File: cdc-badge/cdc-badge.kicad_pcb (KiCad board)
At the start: 4 copper layers, 85 x 110 mm, 159 parts, among them J1 USB_C, J2 JST S2B-PH-SM4-TB, J3 Conn_02x20_Odd_Even, J4 Conn_Grove, J5 Conn_02x03_Odd_Even, J6 Conn_01x06, J7 Conn_01x24, Q1 Si1308EDL, Q2 Si1308EDL, SW0 0, SW1 1, SW10 YES, SW11 NO, SW12 power on/reset, SW13 reset, SW14 flash/power off, SW15 MST-22D18G2 3J, SW16 MST-22D18G2 3J, SW17 MS-22D28-G020, SW2 2, SW3 3, SW4 4, SW5 5, SW6 6, SW7 7, SW8 8, SW9 9, U1 ESP32-S3-WROOM-1-N16R8, U2 TCA9535PWR, U3 TR01-C2P-T301, U5 TLV61070ADBVR, U6 BQ25895RTW, U7 USBLC6-2SC6, U8 TLV62569DBV

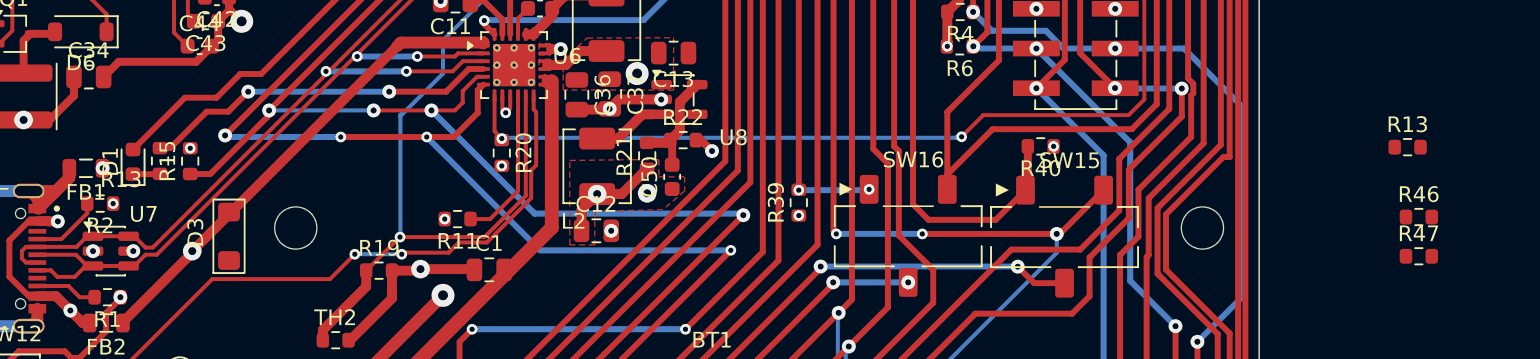
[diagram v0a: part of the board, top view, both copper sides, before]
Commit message: PCB: added R46 and R47 to allow hacking via S3 Pins CE and OTG
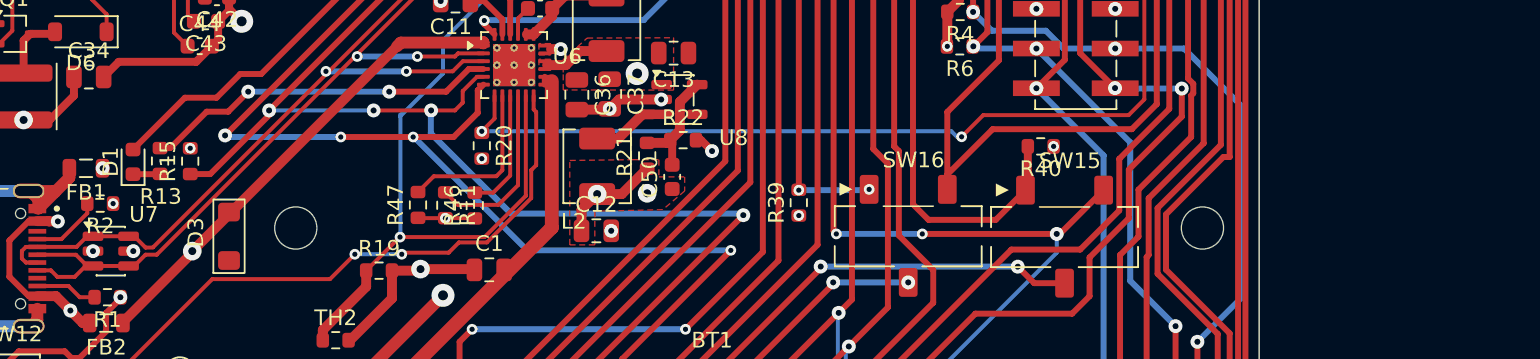
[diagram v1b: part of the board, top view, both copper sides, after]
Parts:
- removed the R13 at (118.2, 90.5)
- moved R47 64.1 mm to (54.9, 94.1), turned to 90 degrees
- moved R46 60.4 mm to (58.6, 94.2), turned to 90 degrees
- moved R20 1.36 mm to (59.0, 90.4)
- moved R11 1.18 mm to (56.7, 94.2), turned to -90 degrees
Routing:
- net Net-(U6-OTG): track 0.00 -> 10.7 mm
- net Net-(U6-~{CE}): track 0.00 -> 7.83 mm
- net Net-(U6-ILIM): track 9.88 -> 11.2 mm
- net GND: track 152.4 -> 153.7 mm, vias 38 -> 37
- net /CHG_IRQ: track 75.9 -> 76.9 mm
- net /I2C0_SCL: track 141.2 -> 142.1 mm
- net /I2C0_SDA: track 132.5 -> 133.3 mm

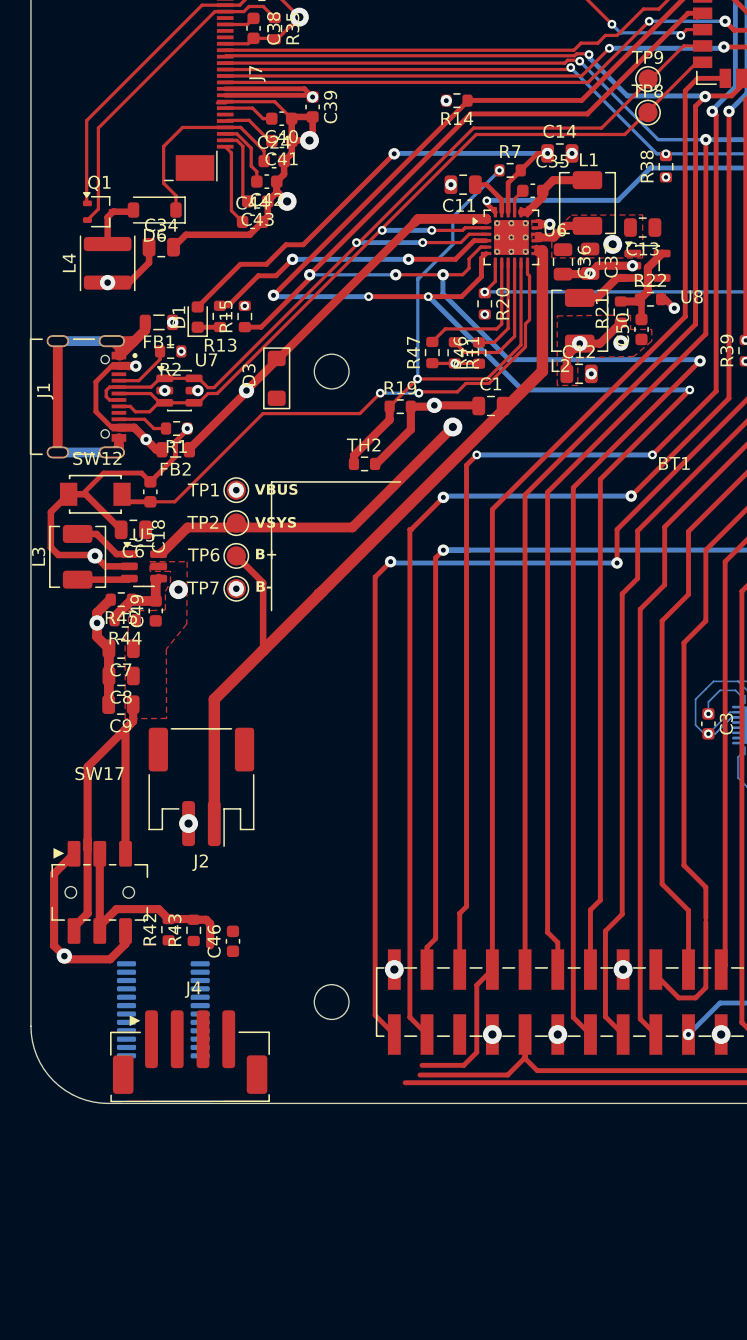
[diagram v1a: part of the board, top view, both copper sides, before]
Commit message: PCB: placed additional diodes and R's to Epaper connector
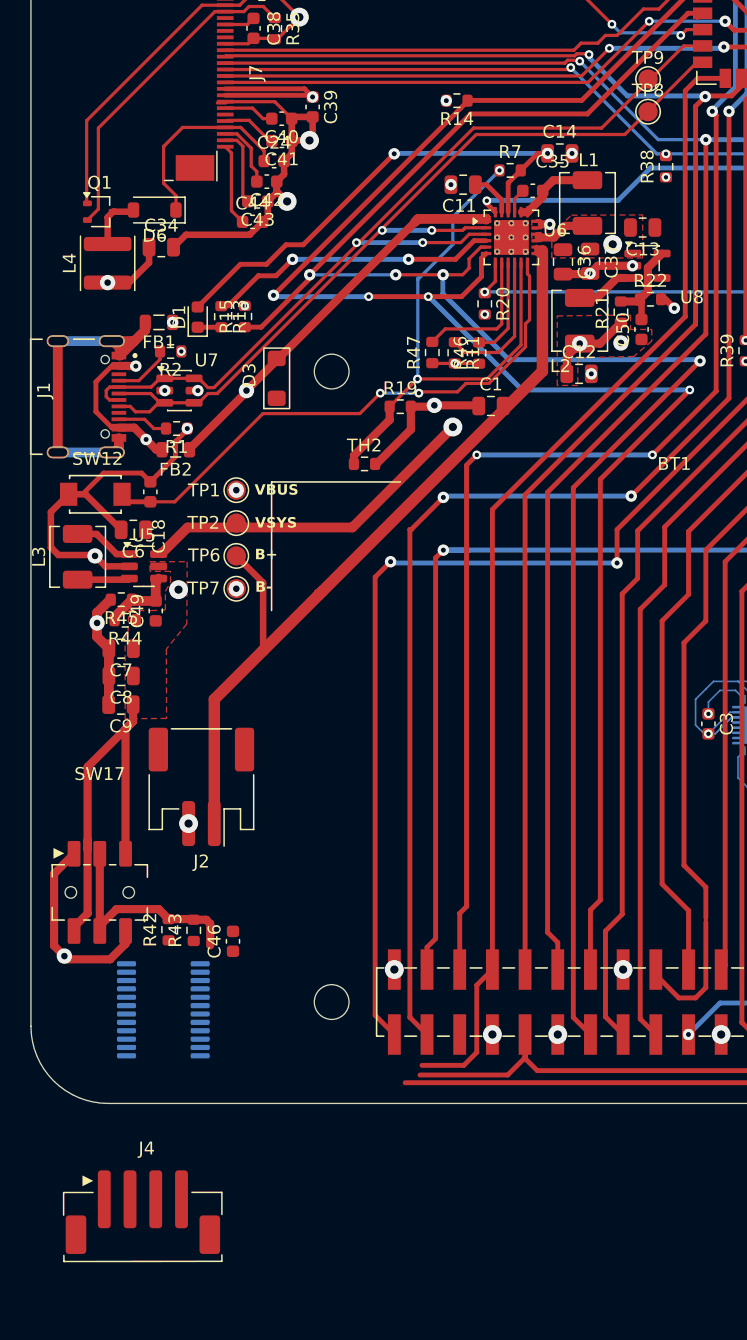
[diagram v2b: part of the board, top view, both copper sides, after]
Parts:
- R13: value 130 -> 5.1k
- moved J4 13.0 mm to (32.5, 162.1)
- moved R13 0.11 mm to (38.5, 91.4), turned to -90 degrees
- moved TP8 0.07 mm to (71.7, 75.4)
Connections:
- R13 pad 1: Net-(D1-K) -> Net-(U6-STAT)
- R13 pad 2: Net-(U6-STAT) -> Net-(D1-K)

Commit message: PCB: replaced TP for VBUS and Grove switch
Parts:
- moved C23 223.7 mm to (32.8, 86.1), turned to 90 degrees
- moved D5 223.0 mm to (35.3, 86.7), turned to 90 degrees
- moved D2 220.3 mm to (37.7, 84.2), turned to 90 degrees
- moved C34 6.55 mm to (29.0, 90.3)
- moved R43 5.02 mm to (40.4, 136.0)
- moved R42 4.56 mm to (37.9, 136.0)
- moved SW17 1.79 mm to (30.9, 136.2)
- moved L4 0.41 mm to (29.4, 86.9)
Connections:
- TP1 pad 1: Net-(FB2-Pad2) -> VBUS
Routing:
- net +3.3V: track 60.9 -> 43.0 mm
- net Net-(J4-VCC): track 17.7 -> 6.00 mm
- net /PREVGL: track 6.01 -> 17.1 mm
- net Net-(FB2-Pad2): track 27.0 -> 18.3 mm, vias 3 -> 2
- net VBUS: track 34.4 -> 42.5 mm, vias 2 -> 3
- net GND: track 153.7 -> 146.0 mm, vias 37 -> 39
- net Net-(D2-K): track 0.00 -> 6.04 mm
- net Net-(D6-A): track 4.51 -> 6.81 mm
- net +5V: track 111.4 -> 109.4 mm

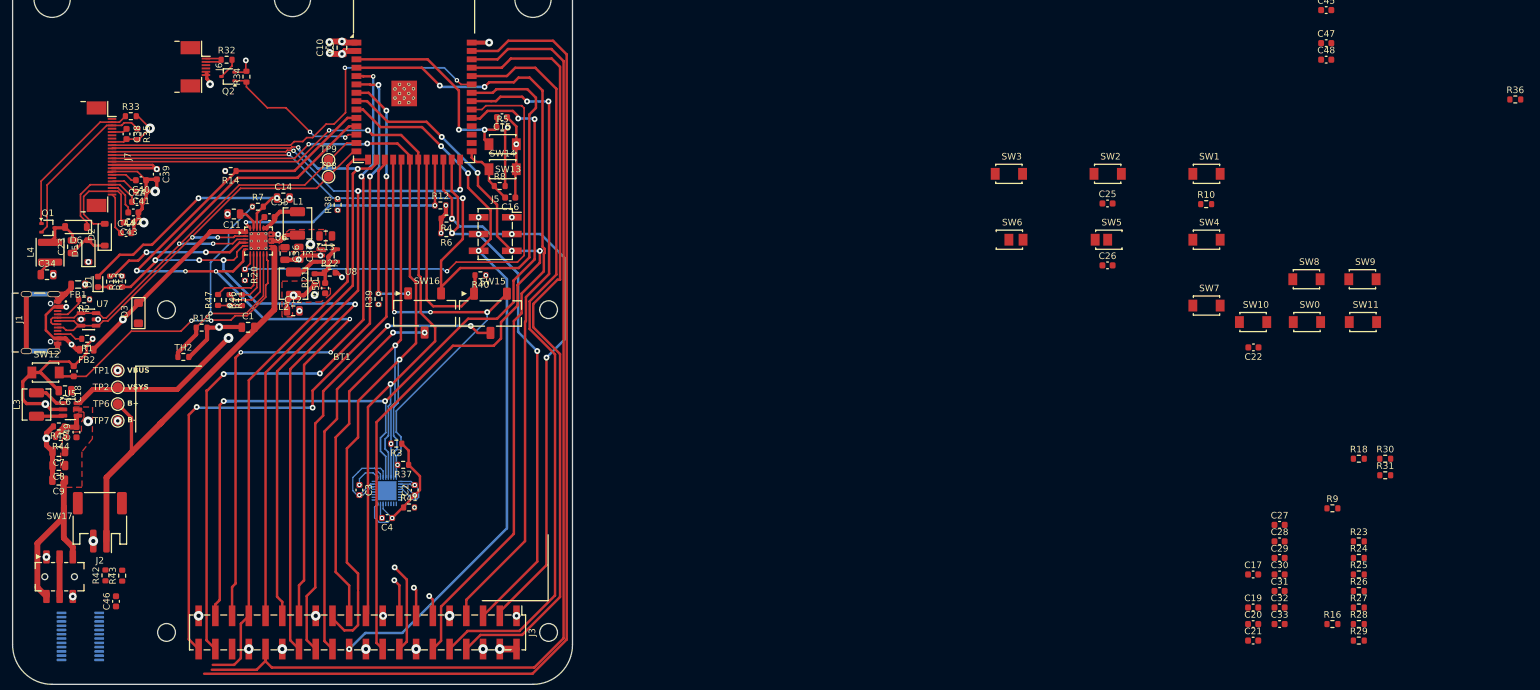
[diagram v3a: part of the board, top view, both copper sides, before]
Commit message: Schematic: PRE_VBUS Netlabel, PCB: review wiring and placement
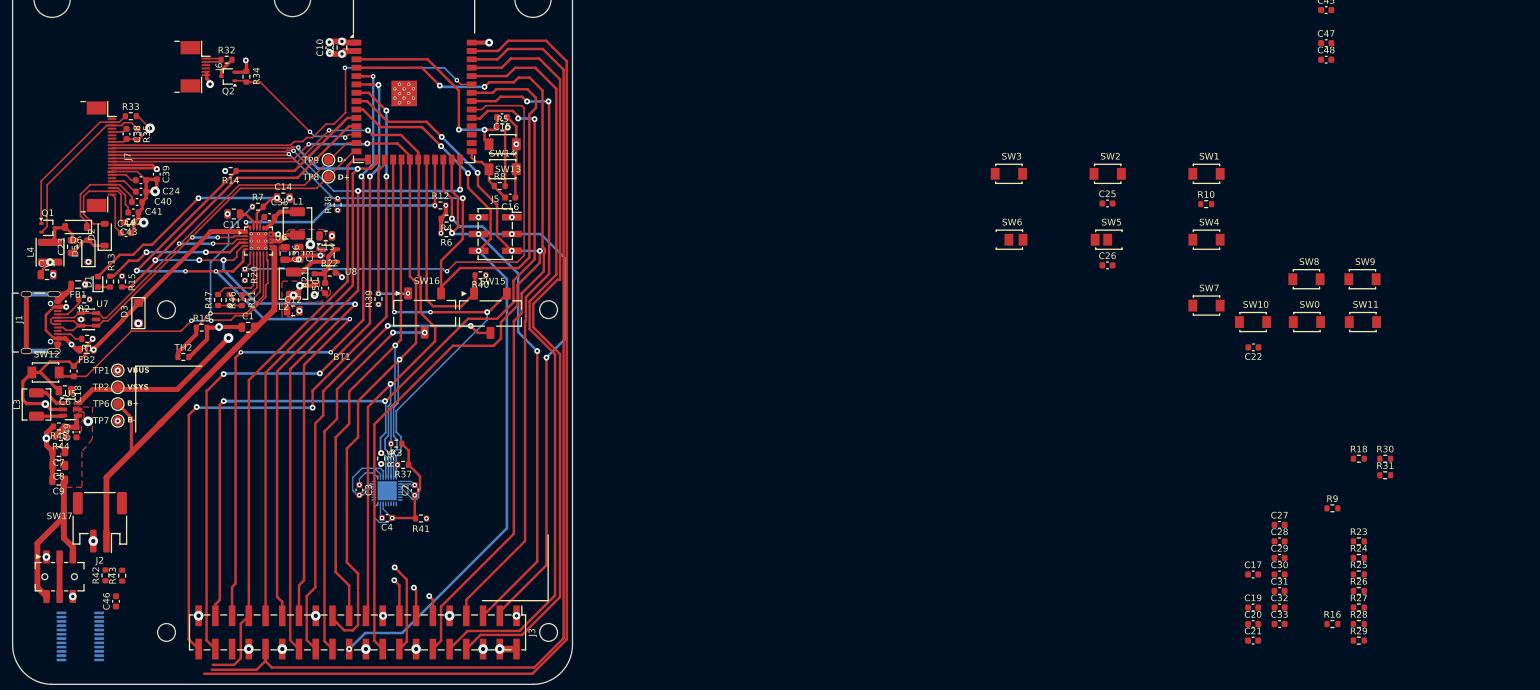
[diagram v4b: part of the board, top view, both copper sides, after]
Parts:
- moved R36 180.6 mm to (79.7, 118.2), turned to -90 degrees
- moved R41 2.47 mm to (85.8, 127.3)
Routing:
- net VBUS: track 42.5 -> 35.6 mm, vias 3 -> 2
- net Net-(U3-PULLUP): track 38.6 -> 40.9 mm
- net /TXD: track 116.1 -> 115.0 mm
- net /GROVE0: track 162.8 -> 162.1 mm
- net /EXP_IRQ: track 161.9 -> 161.3 mm
- net +3.3V: track 43.0 -> 43.3 mm, vias 21 -> 23
- net GND: track 146.0 -> 146.1 mm, vias 39 -> 42
- net /TR01_IRQ: vias 4 -> 5
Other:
- board text added: "D+"
- board text added: "D-"

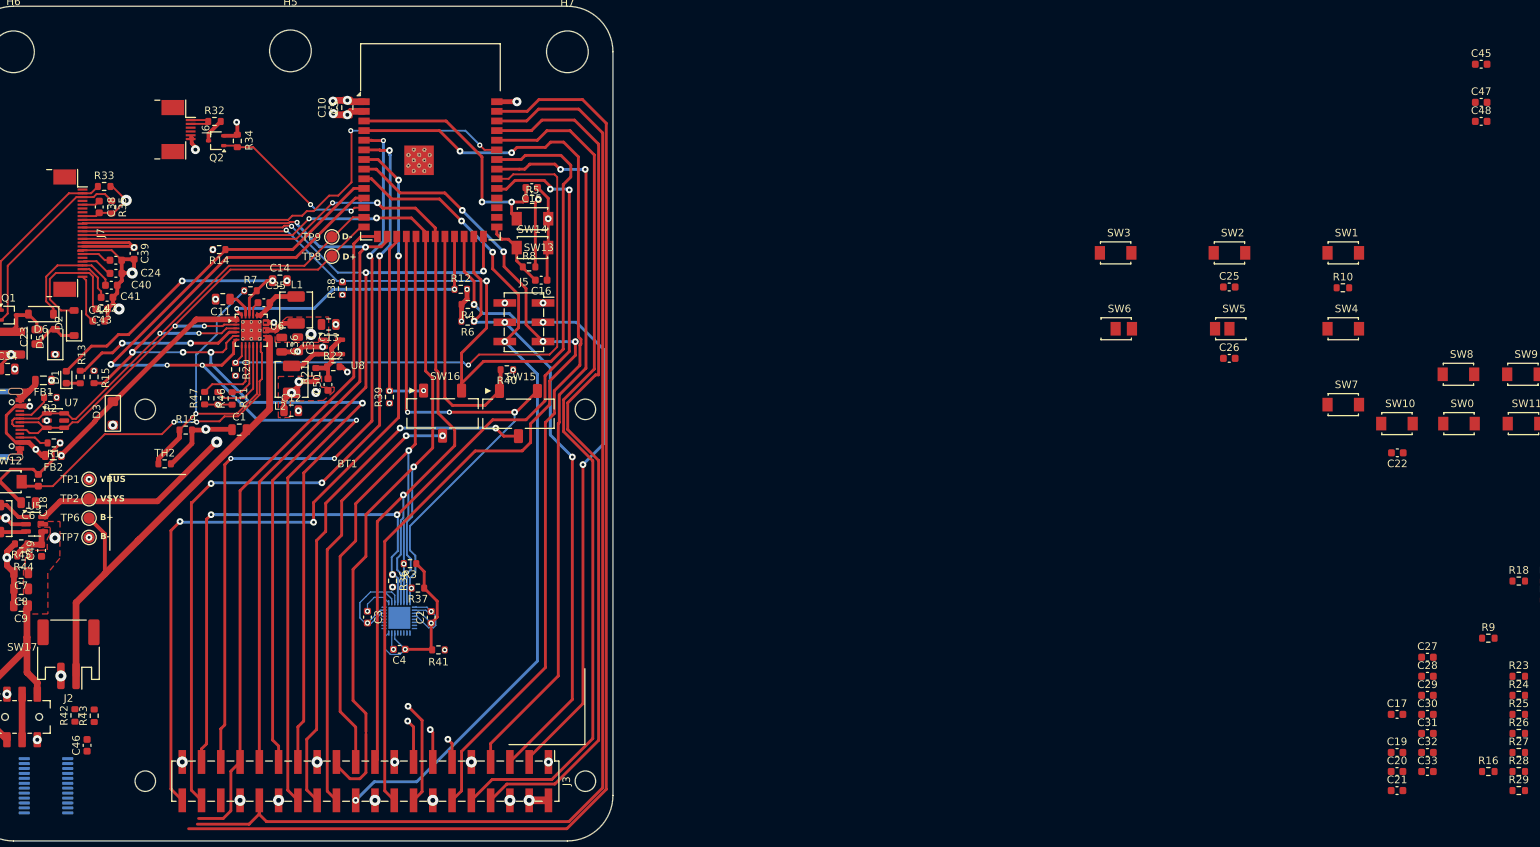
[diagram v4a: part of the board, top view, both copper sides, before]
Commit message: PCB: Placed Caps for Raspi Header 3.3V and 5V, SAO Port and Grove Caps
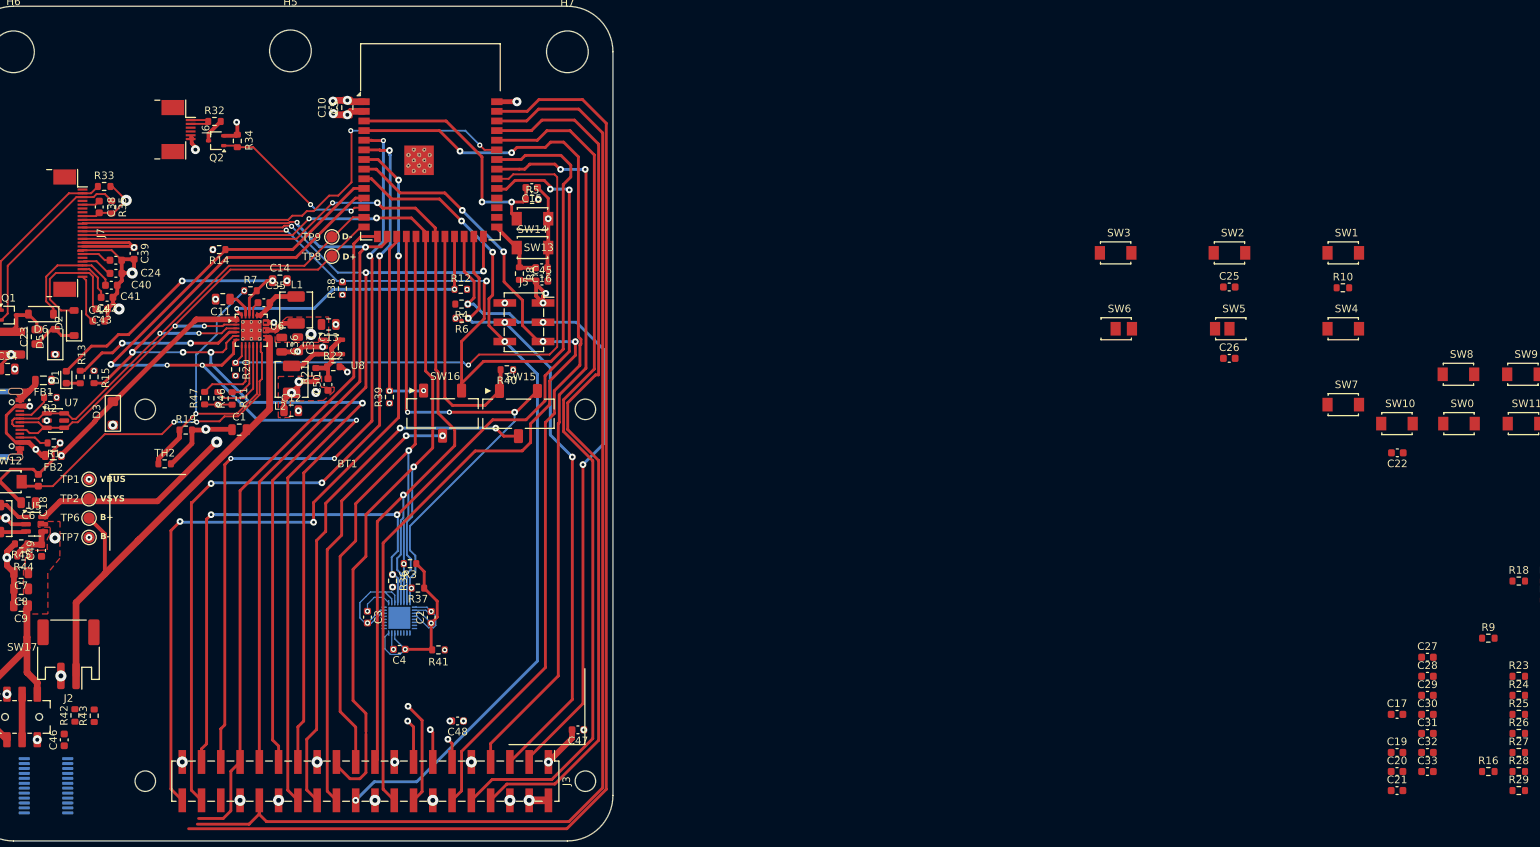
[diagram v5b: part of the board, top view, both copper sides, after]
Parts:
- moved C48 156.3 mm to (88.3, 136.7), turned to 180 degrees
- moved C47 144.9 mm to (104.1, 137.9), turned to 180 degrees
- moved C45 127.0 mm to (99.4, 78.7)
- moved C46 3.09 mm to (36.4, 139.2)
- moved C16 1.64 mm to (99.3, 77.0)
- moved R8 1.55 mm to (96.4, 77.7), turned to -90 degrees
- moved R6 0.86 mm to (88.8, 83.6)
- moved R4 0.83 mm to (88.8, 81.8)
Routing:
- net /I2C1_SDA: track 87.5 -> 88.7 mm
- net /SAO_GPIO2: track 110.3 -> 109.2 mm
- net +3.3V: track 43.3 -> 44.4 mm, vias 23 -> 24
- net Net-(U1-IO0): track 9.63 -> 8.72 mm
- net /I2C1_SCL: track 81.1 -> 81.8 mm
- net /SAO_GPIO1: track 116.0 -> 116.6 mm
- net GND: track 146.1 -> 146.4 mm, vias 42 -> 44
- net +5V: vias 2 -> 3
